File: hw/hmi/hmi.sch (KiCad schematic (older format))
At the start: 60 parts, among them J1 SWD, J2 INTERFACE, J4 SSD1963_LCD, J5 USB, J6 Antenna, Q1 BC847, U1 STM32F412VETx, U2 USB6B1, U3 RFM69HW, U4 MCP2562-E-SN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

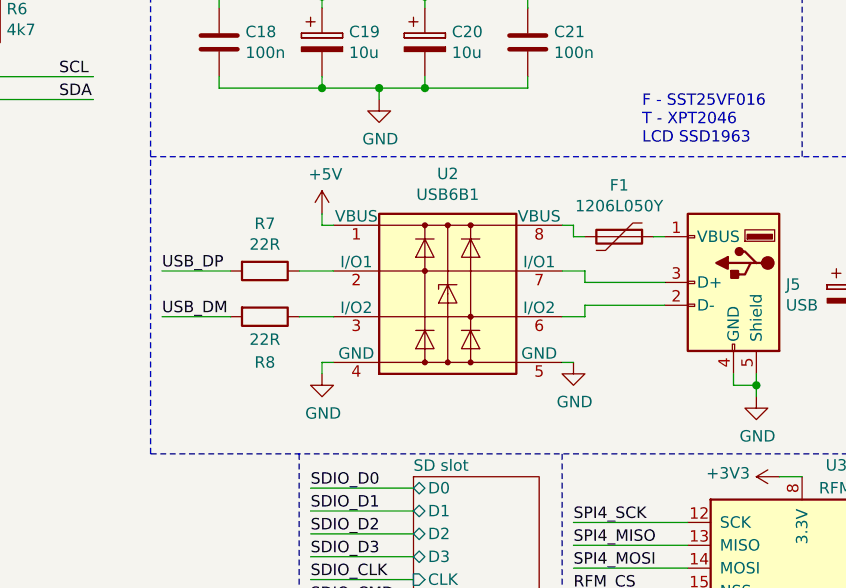
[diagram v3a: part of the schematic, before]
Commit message: Updated schematic to latest changes in usb protection ic
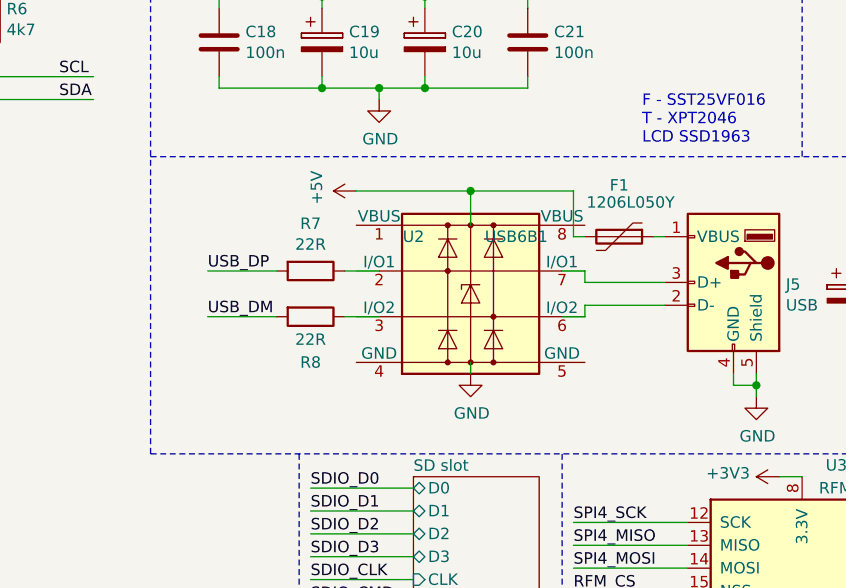
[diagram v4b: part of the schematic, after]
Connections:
- wire segments 395 -> 393
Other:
- moved on the sheet: R7, R8, U2
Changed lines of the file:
@@
 L Power_Protection:USB6B1 U2
 U 1 1 5C210952
-P 6850 4450
-F 0 "U2" H 6850 4975 50  0000 C CNN
-F 1 "USB6B1" H 6850 4884 50  0000 C CNN
-F 2 "Package_SO:SOIC-8_3.9x4.9mm_P1.27mm" H 5875 4050 50  0001 C CNN
-F 3 "http://www.st.com/content/ccc/resource/technical/document/datasheet/3e/ec/b2/54/b2/76/47/90/CD00001361.pdf/files/CD00001361.pdf/jcr:content/translations/en.CD00001361.pdf" H 5900 4350 50  0001 C CNN
-	1    6850 4450
+P 6950 4450
+F 0 "U2" H 6700 4700 50  0000 C CNN
+F 1 "USB6B1" H 7150 4700 50  0000 C CNN
+F 2 "Package_SO:SOIC-8_3.9x4.9mm_P1.27mm" H 5975 4050 50  0001 C CNN
+F 3 "http://www.st.com/content/ccc/resource/technical/document/datasheet/3e/ec/b2/54/b2/76/47/90/CD00001361.pdf/files/CD00001361.pdf/jcr:content/translations/en.CD00001361.pdf" H 6000 4350 50  0001 C CNN
+	1    6950 4450
 	1    0    0    -1
 $EndComp
@@
 Wire Wire Line
 	7450 4550 7350 4550
-$Comp
-L power:GND #PWR0126
-U 1 1 5C247BD7
-P 7400 4750
-F 0 "#PWR0126" H 7400 4500 50  0001 C CNN
-F 1 "GND" H 7405 4577 50  0000 C CNN
-F 2 "" H 7400 4750 50  0001 C CNN
-F 3 "" H 7400 4750 50  0001 C CNN
-	1    7400 4750
-	1    0    0    -1
-$EndComp
-Wire Wire Line
-	7400 4750 7350 4750
-$Comp
-L power:GND #PWR0127
-U 1 1 5C255F6F
-P 6300 4800
-F 0 "#PWR0127" H 6300 4550 50  0001 C CNN
-F 1 "GND" H 6305 4627 50  0000 C CNN
-F 2 "" H 6300 4800 50  0001 C CNN
-F 3 "" H 6300 4800 50  0001 C CNN
-	1    6300 4800
-	1    0    0    -1
-$EndComp
-Wire Wire Line
-	6300 4800 6300 4750
-Wire Wire Line
-	6300 4750 6350 4750
 $Comp
 L power:+5V #PWR0128
 U 1 1 5C26466E
-P 6300 4100
-F 0 "#PWR0128" H 6300 3950 50  0001 C CNN
-F 1 "+5V" H 6315 4273 50  0000 C CNN
-F 2 "" H 6300 4100 50  0001 C CNN
-F 3 "" H 6300 4100 50  0001 C CNN
-	1    6300 4100
-	1    0    0    -1
-$EndComp
-Wire Wire Line
-	6300 4100 6300 4150
-Wire Wire Line
-	6300 4150 6350 4150
+P 6450 4000
+F 0 "#PWR0128" H 6450 3850 50  0001 C CNN
+F 1 "+5V" H 6465 4173 50  0000 C CNN
+F 2 "" H 6450 4000 50  0001 C CNN
+F 3 "" H 6450 4000 50  0001 C CNN
+	1    6450 4000
+	0    -1   -1   0
+$EndComp
 $Comp
 L Device:R R7
 U 1 1 5C273163
-P 6050 4350
-F 0 "R7" V 5843 4350 50  0000 C CNN
-F 1 "22R" V 5934 4350 50  0000 C CNN
-F 2 "Resistor_SMD:R_0805_2012Metric" V 5980 4350 50  0001 C CNN
-F 3 "~" H 6050 4350 50  0001 C CNN
-	1    6050 4350
+P 6250 4350
+F 0 "R7" V 6043 4350 50  0000 C CNN
+F 1 "22R" V 6134 4350 50  0000 C CNN
+F 2 "Resistor_SMD:R_0805_2012Metric" V 6180 4350 50  0001 C CNN
+F 3 "~" H 6250 4350 50  0001 C CNN
+	1    6250 4350
 	0    1    1    0
 $EndComp
@@
 L Device:R R8
 U 1 1 5C27322B
-P 6050 4550
-F 0 "R8" V 6250 4550 50  0000 C CNN
-F 1 "22R" V 6150 4550 50  0000 C CNN
-F 2 "Resistor_SMD:R_0805_2012Metric" V 5980 4550 50  0001 C CNN
-F 3 "~" H 6050 4550 50  0001 C CNN
-	1    6050 4550
+P 6250 4550
+F 0 "R8" V 6450 4550 50  0000 C CNN
+F 1 "22R" V 6350 4550 50  0000 C CNN
+F 2 "Resistor_SMD:R_0805_2012Metric" V 6180 4550 50  0001 C CNN
+F 3 "~" H 6250 4550 50  0001 C CNN
+	1    6250 4550
 	0    1    1    0
 $EndComp
 Wire Wire Line
-	6200 4350 6350 4350
-Wire Wire Line
-	6350 4550 6200 4550
-Wire Wire Line
-	5900 4350 5600 4350
-Text Label 5600 4350 0    50   ~ 0
+	6400 4350 6550 4350
+Wire Wire Line
+	6550 4550 6400 4550
+Wire Wire Line
+	6100 4350 5800 4350
+Text Label 5800 4350 0    50   ~ 0
 USB_DP
 Wire Wire Line
-	5900 4550 5600 4550
-Text Label 5600 4550 0    50   ~ 0
+	6100 4550 5800 4550
+Text Label 5800 4550 0    50   ~ 0
 USB_DM
 Wire Wire Line
@@
 $EndSheet
 Wire Wire Line
-	7400 4150 7350 4150
-Wire Wire Line
 	1950 3100 1350 3100
 Text Label 1350 3100 0    50   ~ 0
@@
 P 7600 4200
 F 0 "F1" V 7375 4200 50  0000 C CNN
-F 1 "1206L050Y" V 7466 4200 50  0000 C CNN
+F 1 "1206L050Y" V 7450 4250 50  0000 C CNN
 F 2 "Fuse:Fuse_1206_3216Metric" H 7650 4000 50  0001 L CNN
 F 3 "~" H 7600 4200 50  0001 C CNN
@@
 Wire Wire Line
 	7750 4200 7800 4200
-Wire Wire Line
-	7400 4150 7400 4200
 Wire Wire Line
 	7400 4200 7450 4200
@@
 Text Label 9350 1650 0    50   ~ 0
 GPS_TX
+Wire Wire Line
+	6450 4000 6950 4000
+Wire Wire Line
+	7400 4000 7400 4200
+Wire Wire Line
+	6950 4150 6950 4000
+Connection ~ 6950 4000
+Wire Wire Line
+	6950 4000 7400 4000
+$Comp
+L power:GND #PWR?
+U 1 1 5C9FFB81
+P 6950 4800
+F 0 "#PWR?" H 6950 4550 50  0001 C CNN
+F 1 "GND" H 6955 4627 50  0000 C CNN
+F 2 "" H 6950 4800 50  0001 C CNN
+F 3 "" H 6950 4800 50  0001 C CNN
+	1    6950 4800
+	1    0    0    -1
+$EndComp
+Wire Wire Line
+	6950 4800 6950 4750
 $EndSCHEMATC
